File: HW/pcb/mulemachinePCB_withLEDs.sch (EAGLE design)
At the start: 31 parts, among them IC1 LD117AV50, IC2 MEGA8-P, J1 DCJ0202, Q1 16Mhz

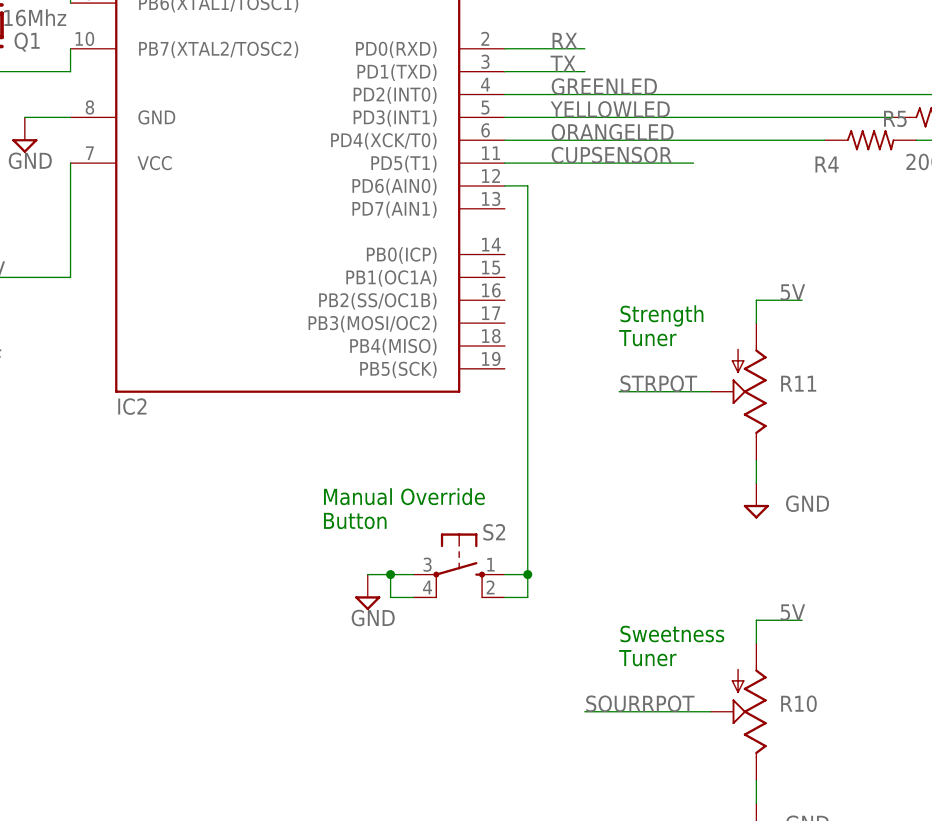
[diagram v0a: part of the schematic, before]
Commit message: finished mating between front panel and PCB. routed PCB. PCB v1.1 is ready for gerber file generation and order.
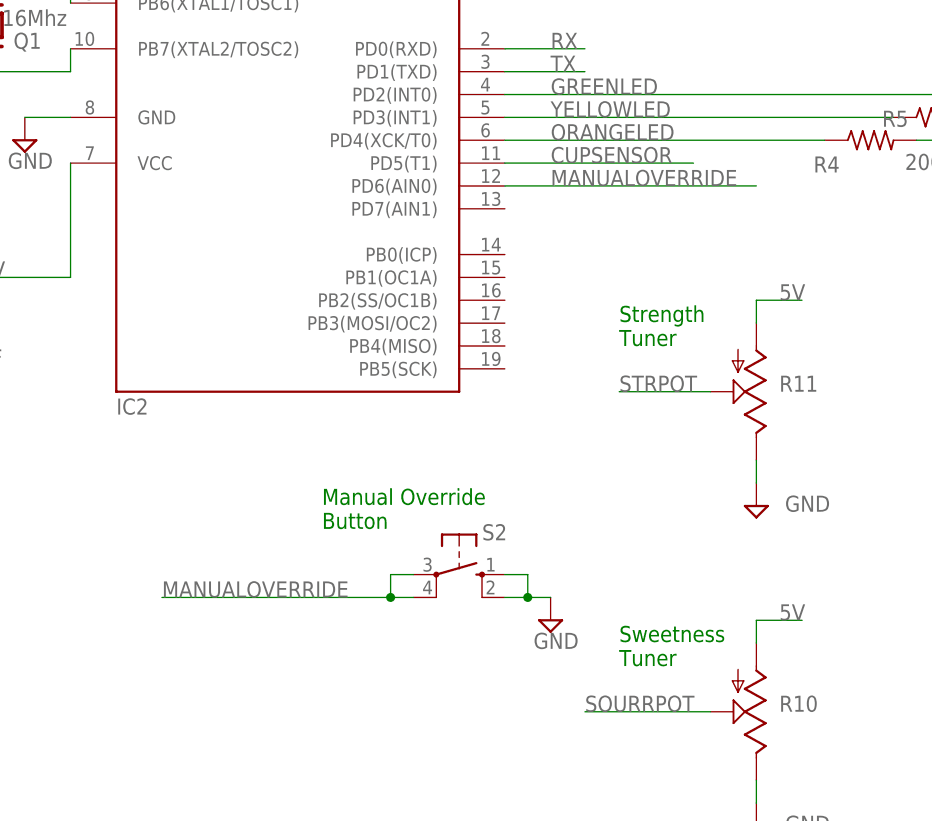
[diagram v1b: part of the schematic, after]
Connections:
- removed net N$24: IC2.PD6(AIN0), S2.S, S2.S1
- new net MANUALOVERRIDE: IC2.PD6(AIN0), S2.P, S2.P1
- net GND: now also S2.S, S2.S1; no longer S2.P, S2.P1
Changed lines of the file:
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@@
 <attribute name="VALUE" x="158.115" y="67.945" size="1.778" layer="96"/>
 </instance>
-<instance part="SUPPLY7" gate="GND" x="58.42" y="0" smashed="yes">
-<attribute name="VALUE" x="56.515" y="-3.175" size="1.778" layer="96"/>
+<instance part="SUPPLY7" gate="GND" x="78.74" y="-2.54" smashed="yes">
+<attribute name="VALUE" x="76.835" y="-5.715" size="1.778" layer="96"/>
 </instance>
 <instance part="SUPPLY8" gate="GND" x="147.32" y="-2.54" smashed="yes">
@@
 </segment>
 <segment>
-<pinref part="SUPPLY7" gate="GND" pin="GND"/>
-<wire x1="58.42" y1="2.54" x2="60.96" y2="2.54" width="0.1524" layer="91"/>
-<pinref part="S2" gate="1" pin="P"/>
-<pinref part="S2" gate="1" pin="P1"/>
-<wire x1="60.96" y1="2.54" x2="63.5" y2="2.54" width="0.1524" layer="91"/>
-<wire x1="63.5" y1="0" x2="60.96" y2="0" width="0.1524" layer="91"/>
-<wire x1="60.96" y1="0" x2="60.96" y2="2.54" width="0.1524" layer="91"/>
-<junction x="60.96" y="2.54"/>
-</segment>
-<segment>
 <pinref part="IC2" gate="G$1" pin="GND"/>
 <wire x1="0" y1="78.74" x2="7.62" y2="78.74" width="0.1524" layer="91"/>
@@
 <pinref part="IC2" gate="G$1" pin="GND@1"/>
 <wire x1="20.32" y1="53.34" x2="25.4" y2="53.34" width="0.1524" layer="91"/>
+</segment>
+<segment>
+<pinref part="S2" gate="1" pin="S"/>
+<wire x1="73.66" y1="2.54" x2="76.2" y2="2.54" width="0.1524" layer="91"/>
+<wire x1="76.2" y1="2.54" x2="76.2" y2="0" width="0.1524" layer="91"/>
+<pinref part="S2" gate="1" pin="S1"/>
+<wire x1="76.2" y1="0" x2="73.66" y2="0" width="0.1524" layer="91"/>
+<pinref part="SUPPLY7" gate="GND" pin="GND"/>
+<wire x1="76.2" y1="0" x2="78.74" y2="0" width="0.1524" layer="91"/>
+<junction x="76.2" y="0"/>
 </segment>
 </net>
@@
 </segment>
 </net>
-<net name="N$24" class="0">
-<segment>
-<wire x1="73.66" y1="45.72" x2="76.2" y2="45.72" width="0.1524" layer="91"/>
-<wire x1="76.2" y1="45.72" x2="76.2" y2="2.54" width="0.1524" layer="91"/>
-<pinref part="IC2" gate="G$1" pin="PD6(AIN0)"/>
-<pinref part="S2" gate="1" pin="S"/>
-<wire x1="73.66" y1="2.54" x2="76.2" y2="2.54" width="0.1524" layer="91"/>
-<wire x1="76.2" y1="2.54" x2="76.2" y2="0" width="0.1524" layer="91"/>
-<junction x="76.2" y="2.54"/>
-<pinref part="S2" gate="1" pin="S1"/>
-<wire x1="76.2" y1="0" x2="73.66" y2="0" width="0.1524" layer="91"/>
-</segment>
-</net>
 <net name="N$12" class="0">
 <segment>
@@
 </segment>
 </net>
+<net name="MANUALOVERRIDE" class="0">
+<segment>
+<pinref part="IC2" gate="G$1" pin="PD6(AIN0)"/>
+<wire x1="73.66" y1="45.72" x2="101.6" y2="45.72" width="0.1524" layer="91"/>
+<label x="78.74" y="45.72" size="1.778" layer="95"/>
+</segment>
+<segment>
+<pinref part="S2" gate="1" pin="P"/>
+<pinref part="S2" gate="1" pin="P1"/>
+<wire x1="60.96" y1="2.54" x2="63.5" y2="2.54" width="0.1524" layer="91"/>
+<wire x1="63.5" y1="0" x2="60.96" y2="0" width="0.1524" layer="91"/>
+<wire x1="60.96" y1="0" x2="60.96" y2="2.54" width="0.1524" layer="91"/>
+<wire x1="60.96" y1="0" x2="35.56" y2="0" width="0.1524" layer="91"/>
+<junction x="60.96" y="0"/>
+<label x="35.56" y="0" size="1.778" layer="95"/>
+</segment>
+</net>
